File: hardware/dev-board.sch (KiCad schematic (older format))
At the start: 8 parts, among them J1 Debug, J2 USB_C_Receptacle_USB2.0, U1 E73-2G4M08S1C

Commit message: Dev Board v1.0.0.0
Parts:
- removed JP1: Jumper, Connector_PinHeader_2.54mm:PinHeader_1x02_P2.54mm_Vertical, symbol Device:Jumper
- J3, J4: renamed from J?; footprint (none) -> Connector_PinHeader_2.54mm:PinHeader_1x18_P2.54mm_Vertical
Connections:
- net labels added: D+, D-, P0.00, P0.02, P0.03, P0.04, P0.05, P0.06, P0.07, P0.08, P0.09, P0.10, P0.11, P0.12, P0.13, P0.15, P0.17, P0.18, P0.20, P0.22, P0.24, P0.26, P0.28, P0.29, P0.30, P0.31, P1.02, P1.04, P1.06, P1.09, P1.10, P1.11, P1.13
- net labels removed: VDD, VDDH
- wire segments 24 -> 26
- no-connect marks 5 -> 4
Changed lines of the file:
@@
 	4200 3000 4500 3000
 Connection ~ 3850 2800
-Text Label 5100 2000 2    50   ~ 0
-VBUS
 $Comp
 L power:GND #PWR01
@@
 $EndComp
 NoConn ~ 2950 3800
-Text Label 5200 2500 1    50   ~ 0
-VDD
-Text Label 5300 2500 1    50   ~ 0
-VDDH
 Text Label 5400 2500 1    50   ~ 0
 DCCH
-Wire Wire Line
-	4800 2000 5100 2000
 $Comp
 L Device:R R1
@@
 $EndComp
 Wire Wire Line
-	5100 2000 5100 2500
-$Comp
-L Device:Jumper JP1
-U 1 1 5ED9687A
-P 4500 2000
-F 0 "JP1" H 4500 2264 50  0000 C CNN
-F 1 "Jumper" H 4500 2173 50  0000 C CNN
-F 2 "Connector_PinHeader_2.54mm:PinHeader_1x02_P2.54mm_Vertical" H 4500 2000 50  0001 C CNN
-F 3 "~" H 4500 2000 50  0001 C CNN
-	1    4500 2000
-	1    0    0    -1
-$EndComp
-Wire Wire Line
-	3900 2000 4200 2000
-Wire Wire Line
-	3900 2300 3900 2000
+	5100 2100 5100 2500
+Wire Wire Line
+	3900 2300 3900 2100
 Wire Wire Line
 	3850 2300 3900 2300
@@
 NoConn ~ 3850 3400
 NoConn ~ 3850 3500
-NoConn ~ 6100 4000
-$Comp
-L Connector:Conn_01x18_Male J?
+$Comp
+L Connector:Conn_01x18_Male J3
 U 1 1 5EDD2C4F
 P 7000 2650
-F 0 "J?" H 7108 3631 50  0000 C CNN
+F 0 "J3" H 7108 3631 50  0000 C CNN
 F 1 "Conn_01x18_Male" H 7108 3540 50  0000 C CNN
-F 2 "" H 7000 2650 50  0001 C CNN
+F 2 "Connector_PinHeader_2.54mm:PinHeader_1x18_P2.54mm_Vertical" H 7000 2650 50  0001 C CNN
 F 3 "~" H 7000 2650 50  0001 C CNN
 	1    7000 2650
@@
 $EndComp
 $Comp
-L Connector:Conn_01x18_Male J?
+L Connector:Conn_01x18_Male J4
 U 1 1 5EDD70F9
 P 7900 2650
-F 0 "J?" H 8008 3631 50  0000 C CNN
+F 0 "J4" H 8008 3631 50  0000 C CNN
 F 1 "Conn_01x18_Male" H 8008 3540 50  0000 C CNN
-F 2 "" H 7900 2650 50  0001 C CNN
+F 2 "Connector_PinHeader_2.54mm:PinHeader_1x18_P2.54mm_Vertical" H 7900 2650 50  0001 C CNN
 F 3 "~" H 7900 2650 50  0001 C CNN
 	1    7900 2650
 	1    0    0    -1
 $EndComp
+Text Label 8100 1850 0    50   ~ 0
+P1.11
+Text Label 4500 4700 2    50   ~ 0
+P1.10
+Text Label 4500 4800 2    50   ~ 0
+P1.11
+Text Label 8100 1950 0    50   ~ 0
+P1.10
+Text Label 6100 3000 0    50   ~ 0
+P0.03
+Text Label 8100 2050 0    50   ~ 0
+P0.03
+Text Label 6100 4600 0    50   ~ 0
+P0.28
+Text Label 8100 2150 0    50   ~ 0
+P0.28
+Text Label 4500 4900 2    50   ~ 0
+P1.13
+Text Label 8100 2250 0    50   ~ 0
+P1.13
+Text Label 6100 2900 0    50   ~ 0
+P0.02
+Text Label 8100 2350 0    50   ~ 0
+P0.02
+Text Label 6100 4700 0    50   ~ 0
+P0.29
+Text Label 8100 2450 0    50   ~ 0
+P0.29
+Text Label 6100 4900 0    50   ~ 0
+P0.31
+Text Label 8100 2550 0    50   ~ 0
+P0.31
+Text Label 6100 4800 0    50   ~ 0
+P0.30
+Text Label 8100 2650 0    50   ~ 0
+P0.30
+Text Label 6100 2700 0    50   ~ 0
+P0.00
+Text Label 8100 2750 0    50   ~ 0
+P0.00
+Text Label 6100 4500 0    50   ~ 0
+P0.26
+Text Label 6100 2800 0    50   ~ 0
+P0.11
+Text Label 8100 2850 0    50   ~ 0
+P0.11
+Text Label 6100 3200 0    50   ~ 0
+P0.05
+Text Label 8100 2950 0    50   ~ 0
+P0.05
+Text Label 4500 4600 2    50   ~ 0
+P1.09
+Text Label 8100 3050 0    50   ~ 0
+P1.09
+Text Label 8100 3150 0    50   ~ 0
+P0.26
+Text Label 6100 3300 0    50   ~ 0
+P0.06
+Text Label 8100 3250 0    50   ~ 0
+P0.06
+Text Label 6100 3500 0    50   ~ 0
+P0.08
+Text Label 8100 3350 0    50   ~ 0
+P0.08
+Text Label 6100 3100 0    50   ~ 0
+P0.04
+Text Label 8100 3450 0    50   ~ 0
+P0.04
+$Comp
+L power:+3.3V #PWR0101
+U 1 1 5EE4B738
+P 5200 2450
+F 0 "#PWR0101" H 5200 2300 50  0001 C CNN
+F 1 "+3.3V" H 5215 2623 50  0000 C CNN
+F 2 "" H 5200 2450 50  0001 C CNN
+F 3 "" H 5200 2450 50  0001 C CNN
+	1    5200 2450
+	1    0    0    -1
+$EndComp
+Wire Wire Line
+	5200 2450 5200 2500
+Wire Wire Line
+	5200 2500 5300 2500
+Connection ~ 5200 2500
+Wire Wire Line
+	3900 2100 5100 2100
+$Comp
+L power:GND #PWR0102
+U 1 1 5EE63A5F
+P 7200 3550
+F 0 "#PWR0102" H 7200 3300 50  0001 C CNN
+F 1 "GND" H 7205 3377 50  0000 C CNN
+F 2 "" H 7200 3550 50  0001 C CNN
+F 3 "" H 7200 3550 50  0001 C CNN
+	1    7200 3550
+	1    0    0    -1
+$EndComp
+Text Label 6100 3800 0    50   ~ 0
+P0.12
+Text Label 8100 3550 0    50   ~ 0
+P0.12
+$Comp
+L power:+3.3V #PWR0103
+U 1 1 5EE67FA8
+P 7550 3450
+F 0 "#PWR0103" H 7550 3300 50  0001 C CNN
+F 1 "+3.3V" H 7565 3623 50  0000 C CNN
+F 2 "" H 7550 3450 50  0001 C CNN
+F 3 "" H 7550 3450 50  0001 C CNN
+	1    7550 3450
+	1    0    0    -1
+$EndComp
+Wire Wire Line
+	7550 3450 7200 3450
+Text Label 6100 3700 0    50   ~ 0
+P0.10
+Text Label 7200 1850 0    50   ~ 0
+P0.10
+Text Label 6100 3600 0    50   ~ 0
+P0.09
+Text Label 7200 1950 0    50   ~ 0
+P0.09
+Text Label 7200 2050 0    50   ~ 0
+SWDCLK
+Text Label 7200 2150 0    50   ~ 0
+SWDIO
+Text Label 6100 4400 0    50   ~ 0
+P0.24
+Text Label 7200 2250 0    50   ~ 0
+P0.24
+Text Label 6100 3900 0    50   ~ 0
+P0.13
+Text Label 7200 2350 0    50   ~ 0
+P0.13
+Text Label 3950 3100 0    50   ~ 0
+D+
+Text Label 3950 2800 0    50   ~ 0
+D-
+Text Label 4900 2100 0    50   ~ 0
+VBUS
+Text Label 4500 3800 2    50   ~ 0
+P0.18
+Text Label 7200 2450 0    50   ~ 0
+P0.18
+Text Label 7200 2550 0    50   ~ 0
+P1.06
+Text Label 7200 2650 0    50   ~ 0
+P1.04
+Text Label 4500 4500 2    50   ~ 0
+P1.06
+Text Label 4500 4400 2    50   ~ 0
+P1.04
+Text Label 4500 4300 2    50   ~ 0
+P1.02
+Text Label 7200 2750 0    50   ~ 0
+P1.02
+Text Label 6100 4300 0    50   ~ 0
+P0.22
+Text Label 7200 2950 0    50   ~ 0
+P0.22
+Text Label 6100 4200 0    50   ~ 0
+P0.20
+Text Label 7200 3050 0    50   ~ 0
+P0.20
+Text Label 6100 4100 0    50   ~ 0
+P0.17
+Text Label 7200 3150 0    50   ~ 0
+P0.17
+Text Label 6100 4000 0    50   ~ 0
+P0.15
+Text Label 7200 3250 0    50   ~ 0
+P0.15
+Text Label 6100 3400 0    50   ~ 0
+P0.07
+Text Label 7200 3350 0    50   ~ 0
+P0.07
+Text Label 7200 2850 0    50   ~ 0
+SWO
 $EndSCHEMATC

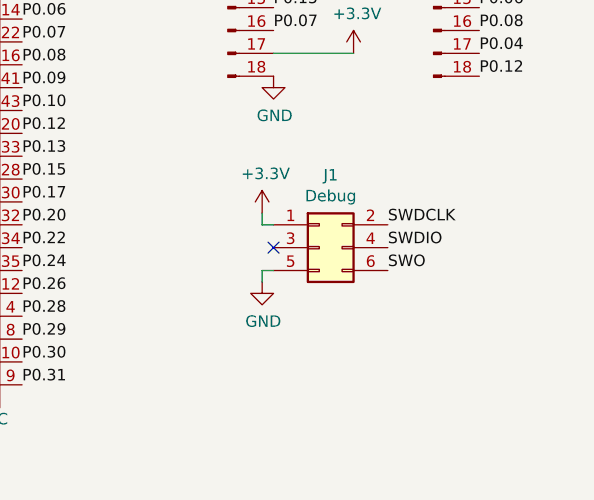
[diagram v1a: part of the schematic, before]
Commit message: Use standard Debug connector (#2) and USB impendance matched (#3)
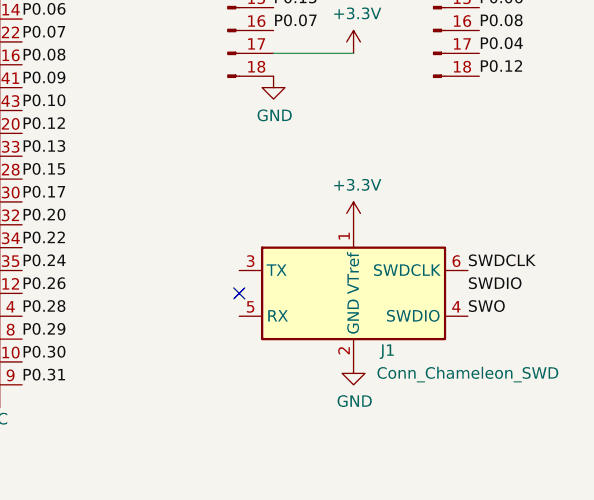
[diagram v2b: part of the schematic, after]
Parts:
- removed J1: Debug, Connector_PinHeader_1.27mm:PinHeader_2x03_P1.27mm_Vertical_SMD, symbol Connector_Generic:Conn_02x03_Odd_Even
- added J1: Conn_Chameleon_SWD, IoT_Home:Chameleon_SWD_Header, symbol IoT_Home:Conn_Chameleon_SWD
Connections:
- net +3V3: now also J1.1 (VTref)
- net GND: now also J1.2 (GND)
- net SWDCLK: now also J1.6 (SWDCLK)
- net SWO: now also J1.4 (SWDIO)
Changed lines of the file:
@@
 Sheet 1 1
 Title "Dev board"
-Date "2020-06-02"
-Rev "1.0.0"
+Date "2020-06-10"
+Rev "1.3.0"
 Comp ""
 Comment1 ""
@@
 	1    0    0    -1
 $EndComp
-$Comp
-L Connector_Generic:Conn_02x03_Odd_Even J1
-U 1 1 5E51628D
-P 7400 4300
-F 0 "J1" H 7450 4617 50  0000 C CNN
-F 1 "Debug" H 7450 4526 50  0000 C CNN
-F 2 "Connector_PinHeader_1.27mm:PinHeader_2x03_P1.27mm_Vertical_SMD" H 7400 4300 50  0001 C CNN
-F 3 "~" H 7400 4300 50  0001 C CNN
-	1    7400 4300
-	1    0    0    -1
-$EndComp
-Text Label 7700 4200 0    50   ~ 0
+Text Label 8050 4400 0    50   ~ 0
 SWDCLK
-Text Label 7700 4300 0    50   ~ 0
+Text Label 8050 4500 0    50   ~ 0
 SWDIO
-Text Label 7700 4400 0    50   ~ 0
+Text Label 8050 4600 0    50   ~ 0
 SWO
-NoConn ~ 7200 4300
 $Comp
 L power:+3.3V #PWR02
 U 1 1 5E51755F
-P 7150 4150
-F 0 "#PWR02" H 7150 4000 50  0001 C CNN
-F 1 "+3.3V" H 7165 4323 50  0000 C CNN
-F 2 "" H 7150 4150 50  0001 C CNN
-F 3 "" H 7150 4150 50  0001 C CNN
-	1    7150 4150
-	1    0    0    -1
-$EndComp
-Wire Wire Line
-	7150 4150 7150 4200
-Wire Wire Line
-	7150 4200 7200 4200
+P 7550 4200
+F 0 "#PWR02" H 7550 4050 50  0001 C CNN
+F 1 "+3.3V" H 7565 4373 50  0000 C CNN
+F 2 "" H 7550 4200 50  0001 C CNN
+F 3 "" H 7550 4200 50  0001 C CNN
+	1    7550 4200
+	1    0    0    -1
+$EndComp
 $Comp
 L power:GND #PWR03
 U 1 1 5E518635
-P 7150 4450
-F 0 "#PWR03" H 7150 4200 50  0001 C CNN
-F 1 "GND" H 7155 4277 50  0000 C CNN
-F 2 "" H 7150 4450 50  0001 C CNN
-F 3 "" H 7150 4450 50  0001 C CNN
-	1    7150 4450
-	1    0    0    -1
-$EndComp
-Wire Wire Line
-	7150 4450 7150 4400
-Wire Wire Line
-	7150 4400 7200 4400
+P 7550 4800
+F 0 "#PWR03" H 7550 4550 50  0001 C CNN
+F 1 "GND" H 7555 4627 50  0000 C CNN
+F 2 "" H 7550 4800 50  0001 C CNN
+F 3 "" H 7550 4800 50  0001 C CNN
+	1    7550 4800
+	1    0    0    -1
+$EndComp
 Text Label 4500 3700 2    50   ~ 0
 SWDCLK
@@
 Text Label 7200 2850 0    50   ~ 0
 SWO
+NoConn ~ 7050 4500
+$Comp
+L IoT_Home:Conn_Chameleon_SWD J1
+U 1 1 5EE0EEC8
+P 7550 4500
+F 0 "J1" H 7700 4250 50  0000 C CNN
+F 1 "Conn_Chameleon_SWD" H 8050 4150 50  0000 C CNN
+F 2 "IoT_Home:Chameleon_SWD_Header" H 7550 4200 50  0001 C CNN
+F 3 "https://github.com/Chameleon-Electronics/programmer-adapter" V 7200 3250 50  0001 C CNN
+	1    7550 4500
+	1    0    0    -1
+$EndComp
 $EndSCHEMATC

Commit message: Release 1.0.0
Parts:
- removed J2: USB_C_Receptacle_USB2.0, Connector_USB:USB_C_Receptacle_Palconn_UTC16-G, symbol Connector:USB_C_Receptacle_USB2.0
- removed R1, R2: 5.1k, Resistor_SMD:R_0805_2012Metric, symbol Device:R
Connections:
- net D+: no longer names the net of U1.31 (D+)
- net D-: no longer names the net of U1.29 (D-)
- net DCCH: no longer names the net of U1.25 (DCCH)
- net VBUS: no longer names the net of U1.27 (VBUS)
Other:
- moved on the sheet: J1, J3, J4, U1

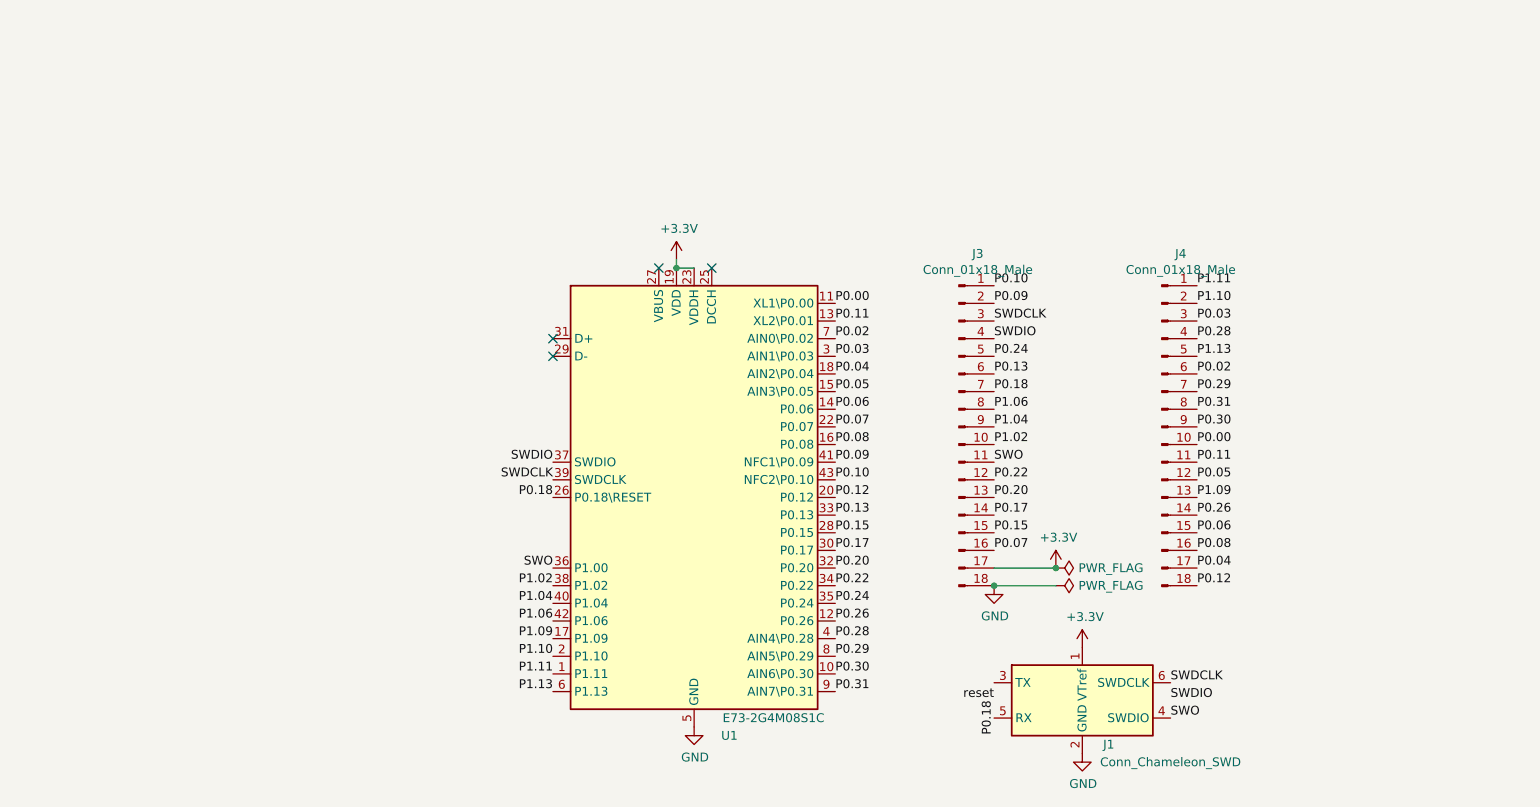
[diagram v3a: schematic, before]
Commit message: nrf52820 schematic
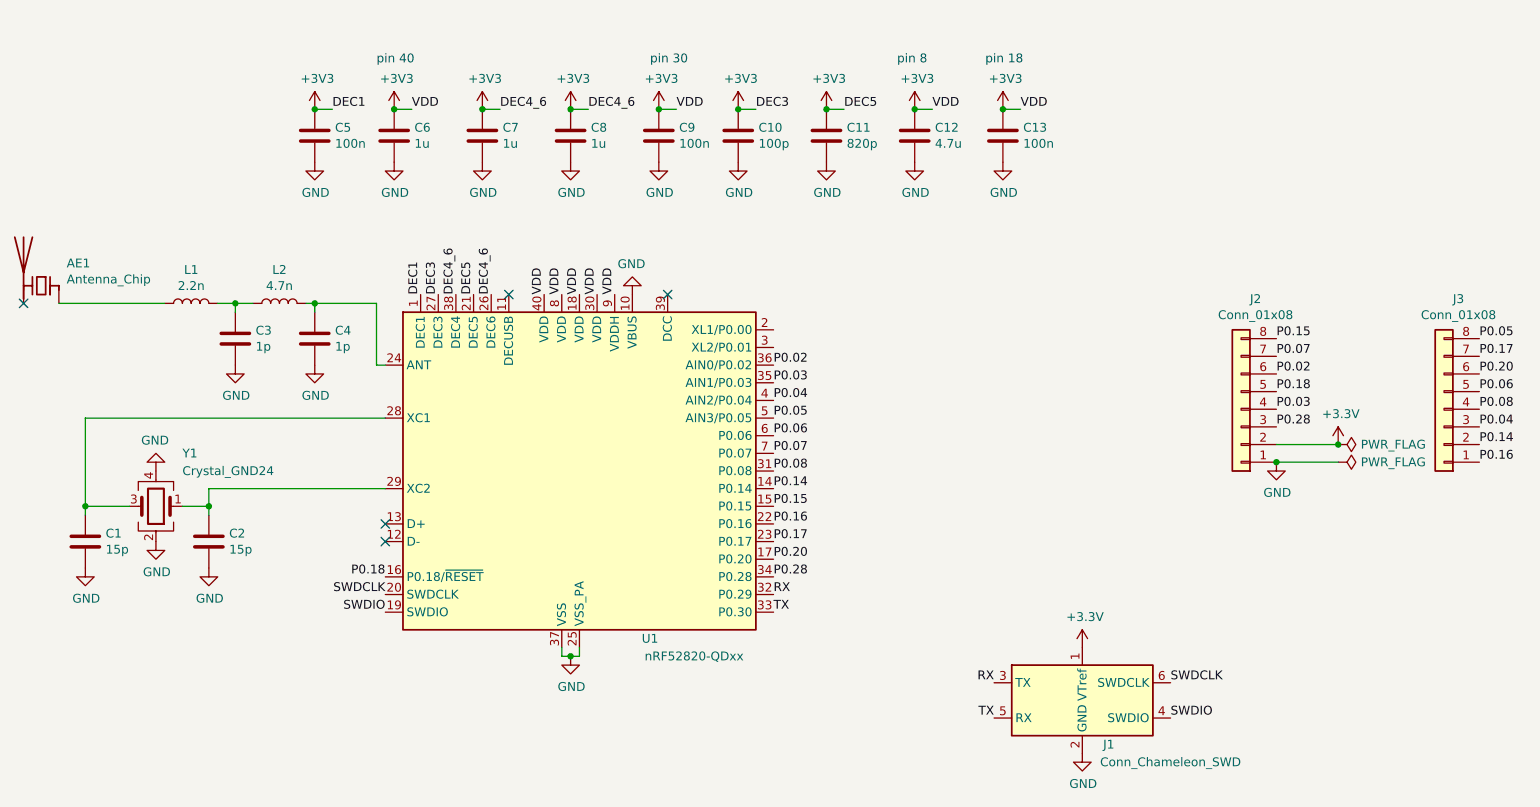
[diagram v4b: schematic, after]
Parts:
- removed J3, J4: Conn_01x18_Male, Connector_PinHeader_2.54mm:PinHeader_1x18_P2.54mm_Vertical, symbol Connector:Conn_01x18_Male
- removed U1: E73-2G4M08S1C, IoT_Home:E73-2G4M08S1C, symbol IoT_Home:E73-2G4M08S1C
- added AE1: Antenna_Chip, RF_Antenna:Johanson_2450AT43F0100, symbol Device:Antenna_Chip
- added C1, C2: 15p, Capacitor_SMD:C_0201_0603Metric, symbol Device:C
- added C10: 100p, Capacitor_SMD:C_0201_0603Metric, symbol Device:C
- added C11: 820p, Capacitor_SMD:C_0201_0603Metric, symbol Device:C
- added C12: 4.7u, Capacitor_SMD:C_0603_1608Metric, symbol Device:C
- added C13, C5, C9: 100n, Capacitor_SMD:C_0201_0603Metric, symbol Device:C
- added C3, C4: 1p, Capacitor_SMD:C_0201_0603Metric, symbol Device:C
- added C6: 1u, Capacitor_SMD:C_0603_1608Metric, symbol Device:C
- added C7, C8: 1u, Capacitor_SMD:C_0402_1005Metric, symbol Device:C
- added J2, J3: Conn_01x08, Connector_PinHeader_2.54mm:PinHeader_1x08_P2.54mm_Vertical, symbol Connector_Generic:Conn_01x08
- added L1: 2.2n, Inductor_SMD:L_0402_1005Metric, symbol Device:L
- added L2: 4.7n, Inductor_SMD:L_0402_1005Metric, symbol Device:L
- added U1: nRF52820-QDxx, Package_DFN_QFN:QFN-40-1EP_5x5mm_P0.4mm_EP3.6x3.6mm_ThermalVias, symbol IoT_Home:nRF52820-QDxx
- added Y1: Crystal_GND24, Crystal:Crystal_SMD_2016-4Pin_2.0x1.6mm, symbol Device:Crystal_GND24
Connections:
- net SWO is gone; now on net SWDIO: J1.4 (SWDIO)
- net +3V3: now also C10.1, C11.1, C12.1, C13.1, C5.1, C6.1, C7.1, C8.1, C9.1, J2.2 (Pin_2), U1.1 (DEC1), U1.18 (VDD), U1.21 (DEC5), U1.26 (DEC6), U1.27 (DEC3), U1.30 (VDD), U1.38 (DEC4), U1.40 (VSS), U1.8 (VDD), U1.9 (VDDH)
- net GND: now also C1.2, C10.2, C11.2, C12.2, C13.2, C2.2, C3.2, C4.2, C5.2, C6.2, C7.2, C8.2, C9.2, J2.1 (Pin_1), U1.10 (VBUS), U1.25 (VSS_PA), U1.37 (VSS), U1.40 (VSS), U1.41 (VSS), Y1.2, Y1.4
- net P0.02: now also J2.6 (Pin_6), U1.36 (AIN0/P0.02)
- net P0.03: now also J2.4 (Pin_4), U1.35 (AIN1/P0.03)
- net P0.04: now also J3.3 (Pin_3), U1.4 (AIN2/P0.04)
- net P0.05: now also J3.8 (Pin_8), U1.5 (AIN3/P0.05)
- net P0.06: now also J3.5 (Pin_5), U1.6 (P0.06)
- net P0.07: now also J2.7 (Pin_7), U1.7 (P0.07)
- net P0.08: now also J3.4 (Pin_4), U1.31 (P0.08)
- net P0.15: now also J2.8 (Pin_8), U1.15 (P0.15)
- net P0.17: now also J3.7 (Pin_7), U1.23 (P0.17)
- net P0.18: now also J2.5 (Pin_5), U1.16 (P0.18/~RESET)
- net P0.20: now also J3.6 (Pin_6), U1.17 (P0.20)
- net P0.28: now also J2.3 (Pin_3), U1.34 (P0.28)
- net SWDCLK: now also U1.20 (SWDCLK)
- net SWDIO: now also U1.19 (SWDIO)
- net RX: now reaches J1.3 (TX)
- net RX: now also U1.32 (P0.29)
- net TX: now reaches J1.5 (RX)
- net TX: now also U1.33 (P0.30)
- new net: C4.1, L2.2, U1.24 (ANT)
- new net: C1.1, U1.28 (XC1), Y1.3
- new net: C2.1, U1.29 (XC2), Y1.1
- new net: C3.1, L1.2, L2.1
- new net: AE1.1 (FEED), L1.1
- new net P0.14: J3.2 (Pin_2), U1.14 (P0.14)
- new net P0.16: J3.1 (Pin_1), U1.22 (P0.16)
- no-connect marks 4 -> 5
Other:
- note added: "pin 18"
- note added: "pin 30"
- note added: "pin 40"
- note added: "pin 8"
